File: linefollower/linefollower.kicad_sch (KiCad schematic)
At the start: 5 parts

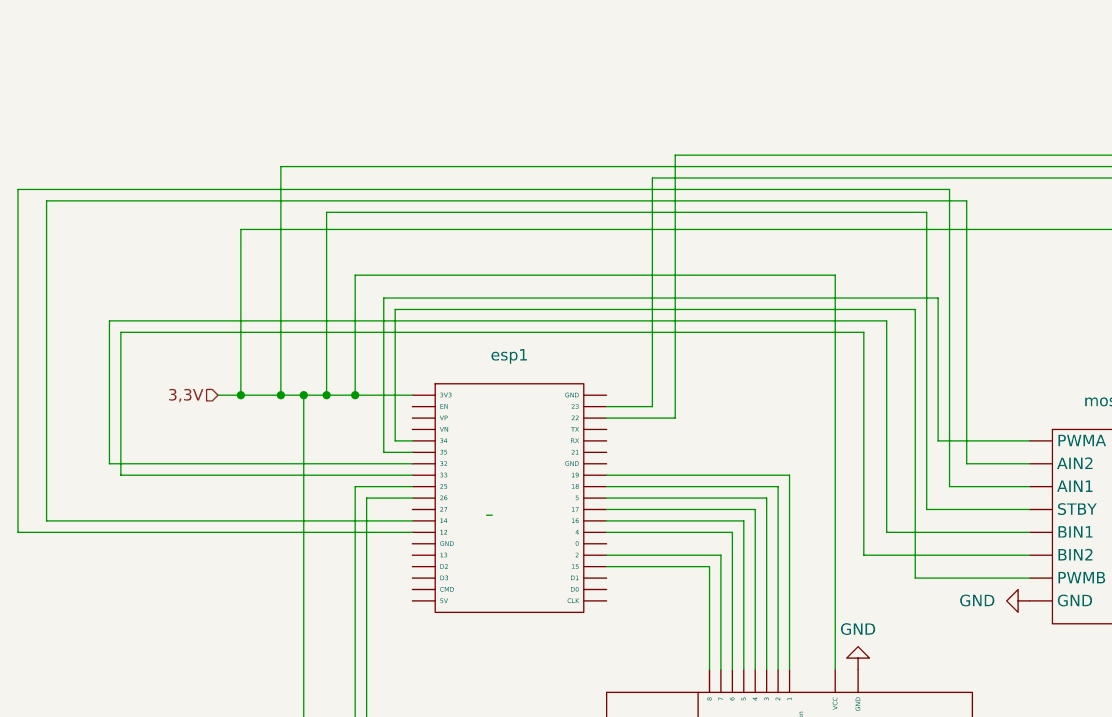
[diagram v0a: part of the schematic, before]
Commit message: Pozamieniane piny
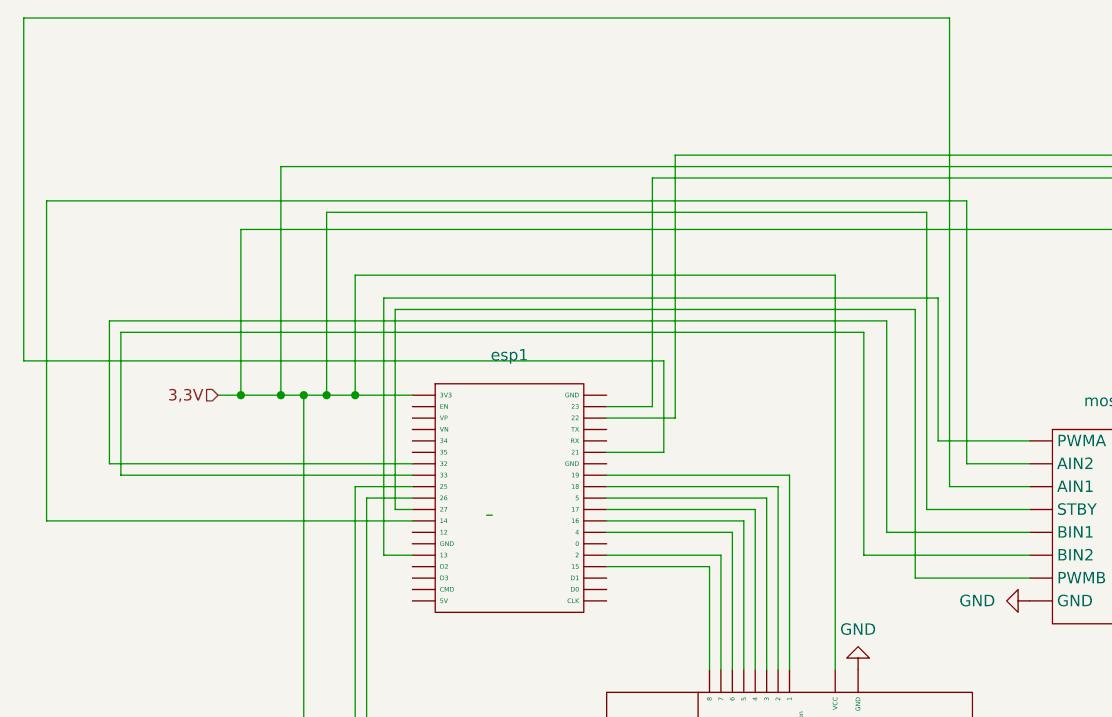
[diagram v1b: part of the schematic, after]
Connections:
- new net: enkoder2. (VCC), esp1. (VP) (x2)
- new net: enkoder1. (VCC), esp1. (VP) (x2)
- new net: esp1. (VP), mostek_h1. (VMOT) (x6)
- new net: QTR_8RC2. (VcC), esp1. (VP) (x8)
- new net: enkoder2. (VCC), mostek_h1. (VMOT) (x2)
- new net: enkoder1. (VCC), mostek_h1. (VMOT) (x2)
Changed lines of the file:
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@@
 	(wire
 		(pts
-			(xy 186.69 17.145) (xy 186.69 50.165)
+			(xy 186.69 -1.905) (xy 186.69 50.165)
 		)
 		(stroke
@@
 	(wire
 		(pts
+			(xy 125.095 52.705) (xy 127 52.705)
+		)
+		(stroke
+			(width 0)
+			(type default)
+		)
+	)
+	(wire
+		(pts
 			(xy 167.64 50.165) (xy 148.59 50.165)
 		)
@@
 	(wire
 		(pts
-			(xy 123.825 46.355) (xy 127 46.355)
-		)
-		(stroke
-			(width 0)
-			(type default)
-		)
-	)
-	(wire
-		(pts
 			(xy 279.4 66.675) (xy 279.4 14.605)
 		)
@@
 	(wire
 		(pts
-			(xy 83.185 17.145) (xy 186.69 17.145)
+			(xy 83.82 -1.905) (xy 186.69 -1.905)
 		)
 		(stroke
@@
 	(wire
 		(pts
-			(xy 83.185 55.245) (xy 83.185 17.145)
+			(xy 83.82 36.195) (xy 83.82 -1.905)
 		)
 		(stroke
@@
 	(wire
 		(pts
+			(xy 123.825 29.21) (xy 123.825 57.785)
+		)
+		(stroke
+			(width 0)
+			(type default)
+		)
+	)
+	(wire
+		(pts
 			(xy 148.59 42.545) (xy 156.21 42.545)
 		)
@@
 	(wire
 		(pts
+			(xy 154.94 46.355) (xy 148.59 46.355)
+		)
+		(stroke
+			(width 0)
+			(type default)
+		)
+	)
+	(wire
+		(pts
 			(xy 269.24 35.56) (xy 269.24 44.45)
 		)
@@
 	(wire
 		(pts
+			(xy 123.825 57.785) (xy 127 57.785)
+		)
+		(stroke
+			(width 0)
+			(type default)
+		)
+	)
+	(wire
+		(pts
 			(xy 173.99 26.67) (xy 120.65 26.67)
 		)
@@
 	(wire
 		(pts
-			(xy 125.095 45.085) (xy 125.095 30.48)
-		)
-		(stroke
-			(width 0)
-			(type default)
-		)
-	)
-	(wire
-		(pts
-			(xy 125.095 45.085) (xy 127 45.085)
+			(xy 125.095 30.48) (xy 125.095 52.705)
 		)
 		(stroke
@@
 	(wire
 		(pts
-			(xy 127 55.245) (xy 83.185 55.245)
+			(xy 83.82 36.195) (xy 154.94 36.195)
 		)
 		(stroke
@@
 	(wire
 		(pts
-			(xy 123.825 29.21) (xy 123.825 46.355)
-		)
-		(stroke
-			(width 0)
-			(type default)
-		)
-	)
-	(wire
-		(pts
 			(xy 264.16 35.56) (xy 264.16 66.675)
 		)
@@
 		)
 	)
+	(wire
+		(pts
+			(xy 154.94 36.195) (xy 154.94 46.355)
+		)
+		(stroke
+			(width 0)
+			(type default)
+		)
+	)
